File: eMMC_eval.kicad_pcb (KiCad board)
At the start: 4 copper layers, 71.1 x 35.6 mm, 13 parts, among them J1 Conn_01x03_Male, J2 Conn_01x04_Male, J3 Conn_01x10_Male, J4 Conn_01x03_Male, J5 Conn_01x10_Male, J6 Conn_01x04_Male, U1 THGBMNG5D1LBAIT

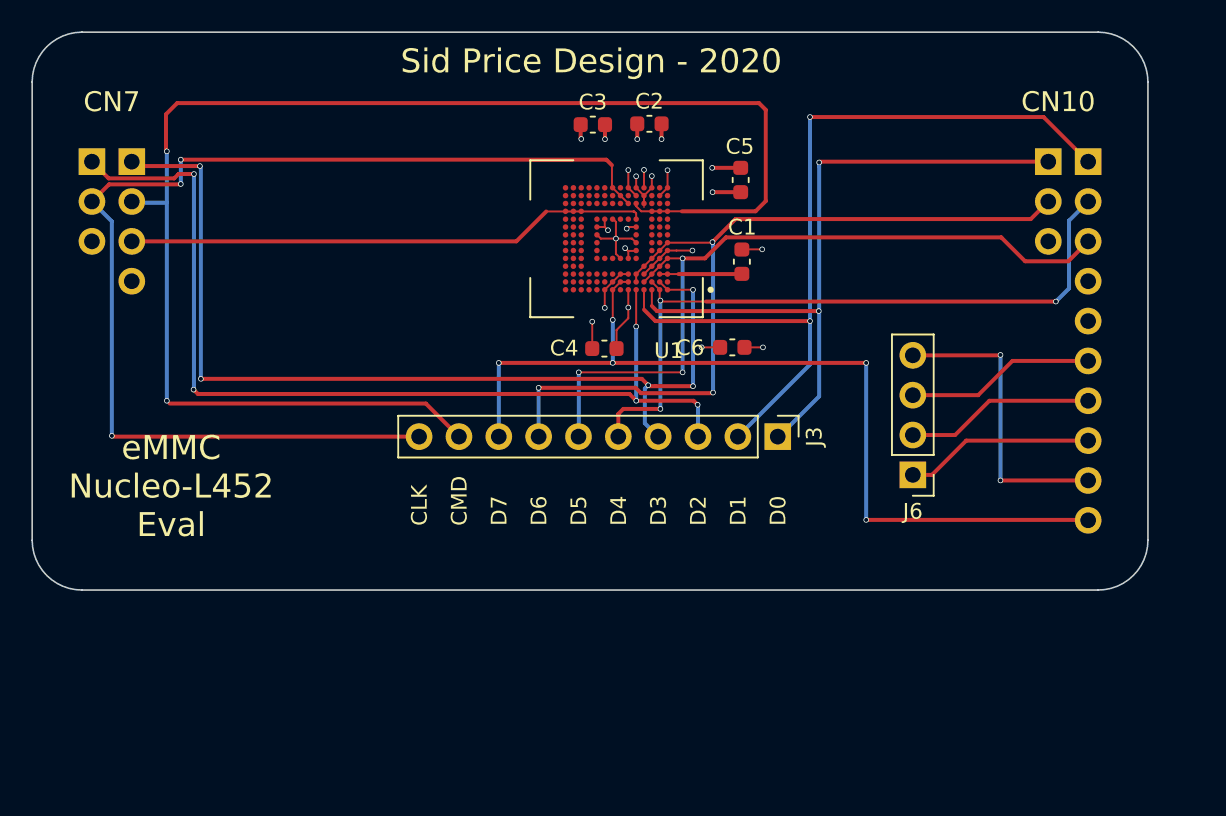
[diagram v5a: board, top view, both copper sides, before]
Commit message: Silk Screen adjustments and additions
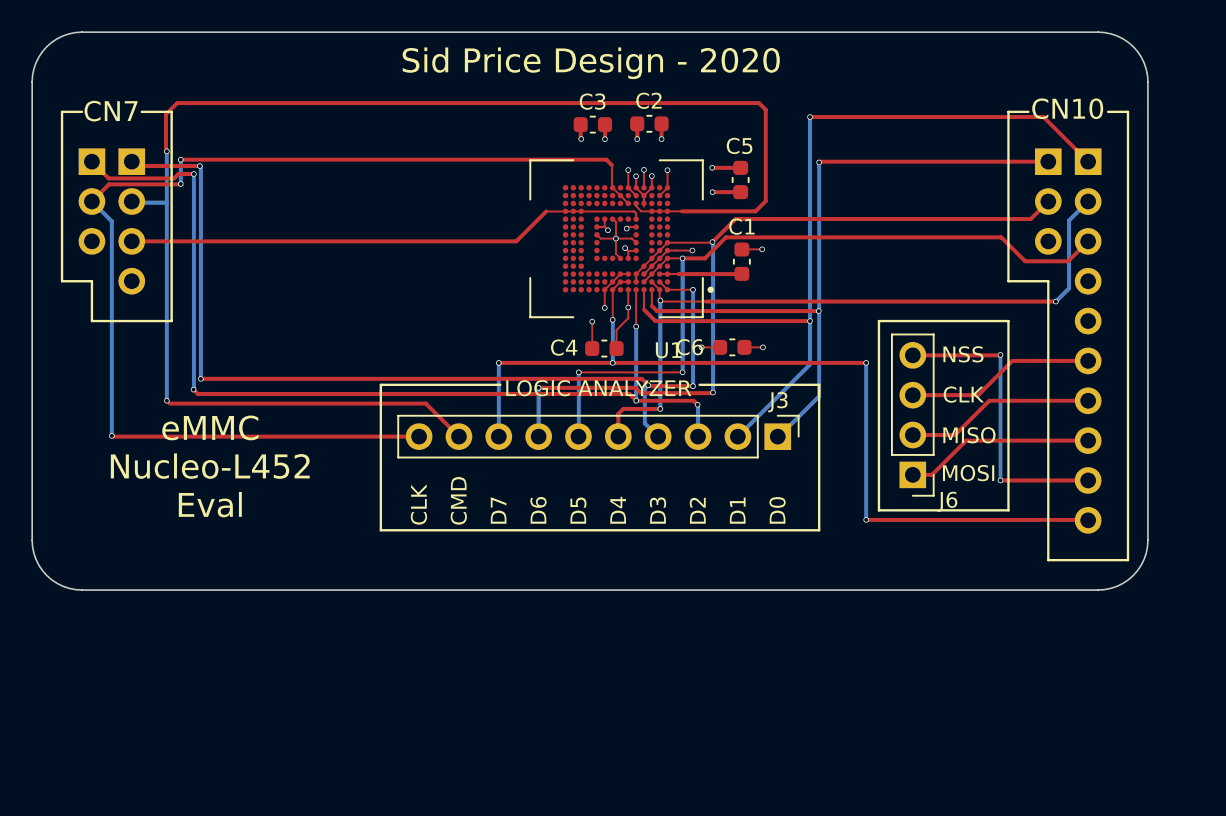
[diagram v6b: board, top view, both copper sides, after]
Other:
- board text added: "LOGIC ANALYZER"
- board text added: "MISO"
- board text added: "MOSI"
- board text added: "NSS"
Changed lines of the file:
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@@
   (general
     (thickness 1.6)
-    (drawings 25)
+    (drawings 55)
     (tracks 289)
     (zones 0)
@@
     (add_net GND)
     (add_net "Net-(C1-Pad1)")
-    (add_net "Net-(J4-Pad3)")
-    (add_net "Net-(J5-Pad4)")
-    (add_net "Net-(J5-Pad5)")
-    (add_net "Net-(U1-PadA10)")
-    (add_net "Net-(U1-PadA11)")
-    (add_net "Net-(U1-PadA12)")
-    (add_net "Net-(U1-PadA13)")
-    (add_net "Net-(U1-PadA14)")
-    (add_net "Net-(U1-PadA7)")
-    (add_net "Net-(U1-PadB1)")
-    (add_net "Net-(U1-PadB10)")
-    (add_net "Net-(U1-PadB11)")
-    (add_net "Net-(U1-PadB12)")
-    (add_net "Net-(U1-PadB13)")
-    (add_net "Net-(U1-PadB14)")
-    (add_net "Net-(U1-PadB9)")
-    (add_net "Net-(U1-PadC10)")
-    (add_net "Net-(U1-PadC11)")
-    (add_net "Net-(U1-PadC12)")
-    (add_net "Net-(U1-PadC13)")
-    (add_net "Net-(U1-PadC14)")
-    (add_net "Net-(U1-PadC8)")
-    (add_net "Net-(U1-PadC9)")
-    (add_net "Net-(U1-PadD1)")
-    (add_net "Net-(U1-PadD12)")
-    (add_net "Net-(U1-PadD13)")
-    (add_net "Net-(U1-PadD14)")
-    (add_net "Net-(U1-PadE10)")
-    (add_net "Net-(U1-PadE12)")
-    (add_net "Net-(U1-PadE13)")
-    (add_net "Net-(U1-PadE14)")
-    (add_net "Net-(U1-PadE5)")
-    (add_net "Net-(U1-PadE8)")
-    (add_net "Net-(U1-PadE9)")
-    (add_net "Net-(U1-PadF10)")
-    (add_net "Net-(U1-PadF12)")
-    (add_net "Net-(U1-PadF13)")
-    (add_net "Net-(U1-PadF14)")
-    (add_net "Net-(U1-PadF3)")
-    (add_net "Net-(U1-PadG10)")
-    (add_net "Net-(U1-PadG12)")
-    (add_net "Net-(U1-PadG13)")
-    (add_net "Net-(U1-PadG14)")
-    (add_net "Net-(U1-PadG2)")
-    (add_net "Net-(U1-PadG3)")
-    (add_net "Net-(U1-PadH1)")
-    (add_net "Net-(U1-PadH12)")
-    (add_net "Net-(U1-PadH13)")
-    (add_net "Net-(U1-PadH14)")
-    (add_net "Net-(U1-PadH2)")
-    (add_net "Net-(U1-PadH3)")
-    (add_net "Net-(U1-PadH5)")
-    (add_net "Net-(U1-PadJ1)")
-    (add_net "Net-(U1-PadJ12)")
-    (add_net "Net-(U1-PadJ13)")
-    (add_net "Net-(U1-PadJ14)")
-    (add_net "Net-(U1-PadJ2)")
-    (add_net "Net-(U1-PadJ3)")
-    (add_net "Net-(U1-PadK1)")
-    (add_net "Net-(U1-PadK10)")
-    (add_net "Net-(U1-PadK12)")
-    (add_net "Net-(U1-PadK13)")
-    (add_net "Net-(U1-PadK14)")
-    (add_net "Net-(U1-PadK2)")
-    (add_net "Net-(U1-PadK3)")
-    (add_net "Net-(U1-PadK6)")
-    (add_net "Net-(U1-PadK7)")
-    (add_net "Net-(U1-PadM1)")
-    (add_net "Net-(U1-PadM10)")
-    (add_net "Net-(U1-PadM11)")
-    (add_net "Net-(U1-PadM12)")
-    (add_net "Net-(U1-PadM13)")
-    (add_net "Net-(U1-PadM14)")
-    (add_net "Net-(U1-PadM2)")
-    (add_net "Net-(U1-PadM3)")
-    (add_net "Net-(U1-PadM7)")
-    (add_net "Net-(U1-PadM8)")
-    (add_net "Net-(U1-PadM9)")
-    (add_net "Net-(U1-PadN1)")
-    (add_net "Net-(U1-PadN10)")
-    (add_net "Net-(U1-PadN11)")
-    (add_net "Net-(U1-PadN12)")
-    (add_net "Net-(U1-PadN13)")
-    (add_net "Net-(U1-PadN14)")
-    (add_net "Net-(U1-PadN3)")
-    (add_net "Net-(U1-PadN6)")
-    (add_net "Net-(U1-PadN8)")
-    (add_net "Net-(U1-PadN9)")
-    (add_net "Net-(U1-PadP10)")
-    (add_net "Net-(U1-PadP11)")
-    (add_net "Net-(U1-PadP12)")
-    (add_net "Net-(U1-PadP13)")
-    (add_net "Net-(U1-PadP14)")
-    (add_net "Net-(U1-PadP2)")
-    (add_net "Net-(U1-PadP7)")
-    (add_net "Net-(U1-PadP9)")
   )
   (module Kicad_Footprints:BGA153N50P14X14_1000X1100X80 (layer F.Cu)
@@
     (descr "Through hole straight pin header, 1x04, 2.54mm pitch, single row")
     (tags "Through hole pin header THT 1x04 2.54mm single row")
-    (fp_text reference J6 (at 0 -2.33) (layer F.SilkS)
+    (fp_text reference J6 (at -2.286 -1.6256) (layer F.SilkS)
       (effects (font (size 1 1) (thickness 0.15)))
     )
@@
     (descr "Through hole straight pin header, 1x10, 2.54mm pitch, single row")
     (tags "Through hole pin header THT 1x10 2.54mm single row")
-    (fp_text reference J3 (at 0 -2.33 90) (layer F.SilkS)
+    (fp_text reference J3 (at -2.286 -0.1016 180) (layer F.SilkS)
       (effects (font (size 1 1) (thickness 0.15)))
     )
@@
     )
   )
+  (gr_line (start 173.355 110.744) (end 173.355 111.125) (layer F.SilkS) (width 0.15))
+  (gr_line (start 145.415 111.125) (end 145.415 110.744) (layer F.SilkS) (width 0.15))
+  (gr_line (start 132.08 93.345) (end 130.175 93.345) (layer F.SilkS) (width 0.15))
+  (gr_line (start 132.08 106.68) (end 132.08 93.345) (layer F.SilkS) (width 0.15))
+  (gr_line (start 127 106.68) (end 132.08 106.68) (layer F.SilkS) (width 0.15))
+  (gr_line (start 127 104.14) (end 127 106.68) (layer F.SilkS) (width 0.15))
+  (gr_line (start 125.095 104.14) (end 127 104.14) (layer F.SilkS) (width 0.15))
+  (gr_line (start 125.095 93.345) (end 125.095 104.14) (layer F.SilkS) (width 0.15))
+  (gr_line (start 126.365 93.345) (end 125.095 93.345) (layer F.SilkS) (width 0.15))
+  (gr_line (start 173.355 110.744) (end 165.735 110.744) (layer F.SilkS) (width 0.15))
+  (gr_line (start 173.355 120.015) (end 173.355 111.125) (layer F.SilkS) (width 0.15))
+  (gr_line (start 145.415 120.015) (end 173.355 120.015) (layer F.SilkS) (width 0.15))
+  (gr_line (start 145.415 111.125) (end 145.415 120.015) (layer F.SilkS) (width 0.15))
+  (gr_line (start 153.035 110.744) (end 145.415 110.744) (layer F.SilkS) (width 0.15))
+  (gr_text "LOGIC ANALYZER" (at 159.258 110.998) (layer F.SilkS)
+    (effects (font (size 1 1) (thickness 0.15)))
+  )
+  (gr_line (start 177.165 118.745) (end 177.165 106.68) (layer F.SilkS) (width 0.15))
+  (gr_line (start 185.42 118.745) (end 177.165 118.745) (layer F.SilkS) (width 0.15))
+  (gr_line (start 185.42 106.68) (end 185.42 118.745) (layer F.SilkS) (width 0.15))
+  (gr_line (start 177.165 106.68) (end 185.42 106.68) (layer F.SilkS) (width 0.15))
+  (gr_line (start 185.42 93.345) (end 186.69 93.345) (layer F.SilkS) (width 0.15))
+  (gr_line (start 185.42 104.14) (end 185.42 93.345) (layer F.SilkS) (width 0.15))
+  (gr_line (start 187.96 104.14) (end 185.42 104.14) (layer F.SilkS) (width 0.15))
+  (gr_line (start 187.96 121.92) (end 187.96 104.14) (layer F.SilkS) (width 0.15))
+  (gr_line (start 193.04 121.92) (end 187.96 121.92) (layer F.SilkS) (width 0.15))
+  (gr_line (start 193.04 93.345) (end 193.04 121.92) (layer F.SilkS) (width 0.15))
+  (gr_line (start 191.77 93.345) (end 193.04 93.345) (layer F.SilkS) (width 0.15))
+  (gr_text NSS (at 182.5244 108.839) (layer F.SilkS)
+    (effects (font (size 1 1) (thickness 0.15)))
+  )
+  (gr_text CLK (at 182.5244 111.4044) (layer F.SilkS)
+    (effects (font (size 1 1) (thickness 0.15)))
+  )
+  (gr_text MISO (at 182.9054 113.9952) (layer F.SilkS)
+    (effects (font (size 1 1) (thickness 0.15)))
+  )
+  (gr_text MOSI (at 182.88 116.4082) (layer F.SilkS)
+    (effects (font (size 1 1) (thickness 0.15)))
+  )
   (gr_text D4 (at 160.5788 119.7356 90) (layer F.SilkS)
     (effects (font (size 1 1) (thickness 0.15)) (justify left))
@@
     (effects (font (size 1 1) (thickness 0.15)) (justify left))
   )
-  (gr_text CN10 (at 188.595 92.71) (layer F.SilkS)
+  (gr_text CN10 (at 189.2046 93.1926) (layer F.SilkS)
     (effects (font (size 1.27 1.27) (thickness 0.15)))
   )
-  (gr_text CN7 (at 128.27 92.71) (layer F.SilkS)
+  (gr_text CN7 (at 128.2446 93.345) (layer F.SilkS)
     (effects (font (size 1.27 1.27) (thickness 0.15)))
   )
@@
     (effects (font (size 1 1) (thickness 0.15)) (justify left))
   )
-  (gr_text "eMMC\nNucleo-L452\nEval" (at 132.0546 117.221) (layer F.SilkS)
+  (gr_text "eMMC\nNucleo-L452\nEval" (at 134.5438 116.0018) (layer F.SilkS)
     (effects (font (size 1.524 1.524) (thickness 0.1778)))
   )

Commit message: Change min track, via, drill to OSHPark specification
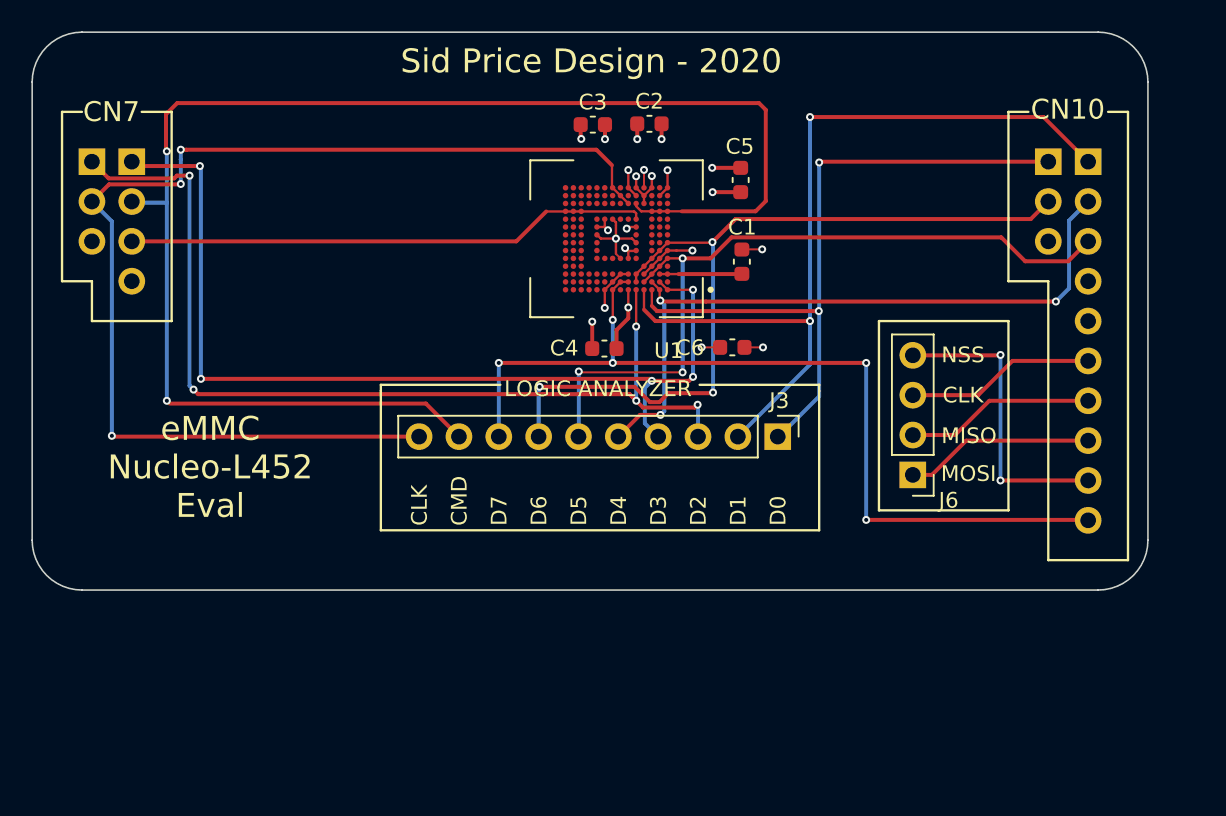
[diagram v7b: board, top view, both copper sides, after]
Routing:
- net /SDMMC1_CK: track 73.2 -> 74.1 mm
- net /SDMMC1_D6: track 52.7 -> 53.2 mm

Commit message: Added pullup resistors and fixed issue with reset input
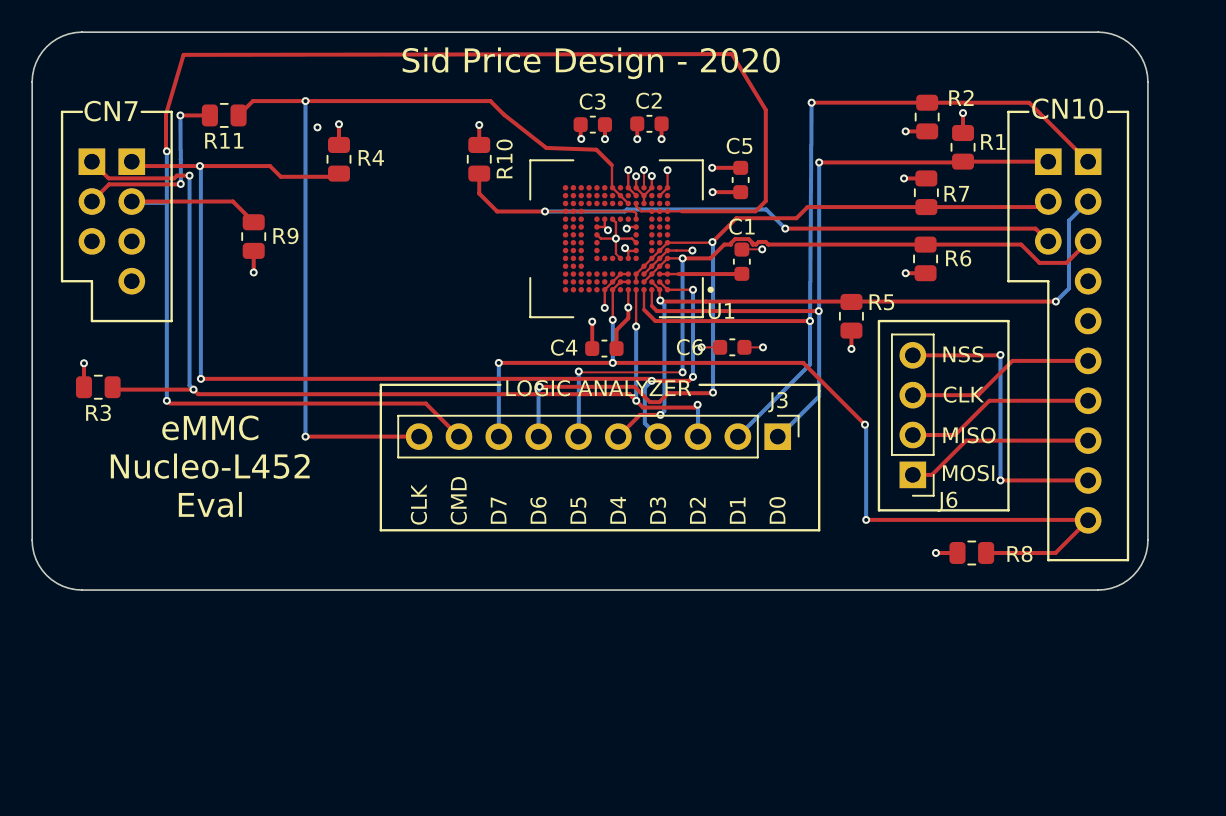
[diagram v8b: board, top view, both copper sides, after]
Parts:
- added R1: 47K, Resistor_SMD:R_0805_2012Metric, F.Cu at (182.5, 95.6)
- added R10: 47K, Resistor_SMD:R_0805_2012Metric, F.Cu at (151.7, 96.4)
- added R11: 33, Resistor_SMD:R_0805_2012Metric, F.Cu at (135.4, 93.6)
- added R2: 47K, Resistor_SMD:R_0805_2012Metric, F.Cu at (180.2, 93.7)
- added R3: 47K, Resistor_SMD:R_0805_2012Metric, F.Cu at (127.4, 110.9)
- added R4: 47K, Resistor_SMD:R_0805_2012Metric, F.Cu at (142.7, 96.4)
- added R5: 47K, Resistor_SMD:R_0805_2012Metric, F.Cu at (175.4, 106.4)
- added R6: 47K, Resistor_SMD:R_0805_2012Metric, F.Cu at (180.1, 102.7)
- added R7: 47K, Resistor_SMD:R_0805_2012Metric, F.Cu at (180.2, 98.5)
- added R8: 47K, Resistor_SMD:R_0805_2012Metric, F.Cu at (183.1, 121.5)
- added R9: 47K, Resistor_SMD:R_0805_2012Metric, F.Cu at (137.3, 101.3)
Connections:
- J2 pad 3: /~SDMMC1_RST -> (no net)
- J3 pad 10: /SDMMC1_CK -> /SDMMC1_CK`
- J4 pad 3: (no net) -> /~SDMMC1_RST
- U1 pad M6: /SDMMC1_CK -> /SDMMC1_CK`
- U1 pad N7: /SDMMC1_CK -> /SDMMC1_CK`
- U1 pad P8: /SDMMC1_CK -> /SDMMC1_CK`
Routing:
- net /SDMMC1_CK: track 74.1 -> 12.4 mm, vias 3 -> 2
- net /SDMMC1_CK`: track 0.00 -> 57.2 mm, vias 0 -> 2
- net +3V3: track 15.6 -> 29.0 mm, vias 10 -> 21
- net /SDMMC1_CMD: track 93.6 -> 106.3 mm
- net /~SDMMC1_RST: track 33.4 -> 45.1 mm, vias 0 -> 2
- net /SDMMC1_D3: track 61.6 -> 70.8 mm
- net /SDMMC1_D2: track 62.3 -> 67.5 mm
- net /SDMMC1_D7: track 58.1 -> 63.2 mm
- net /SDMMC1_D1: track 53.3 -> 54.5 mm
